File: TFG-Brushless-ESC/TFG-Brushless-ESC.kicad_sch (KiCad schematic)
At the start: 50 parts, among them J1 24V IN, J2 U, J3 V, J4 W, J5 USB C Receptacle, J6 HALL SENSORS, J7 SWD, SW1 BOOT0, SW2 NRST, U1 LM317, U2 LM317, U3 STM32F411CEUx, Y1 25MHz, Y2 32.768kHz

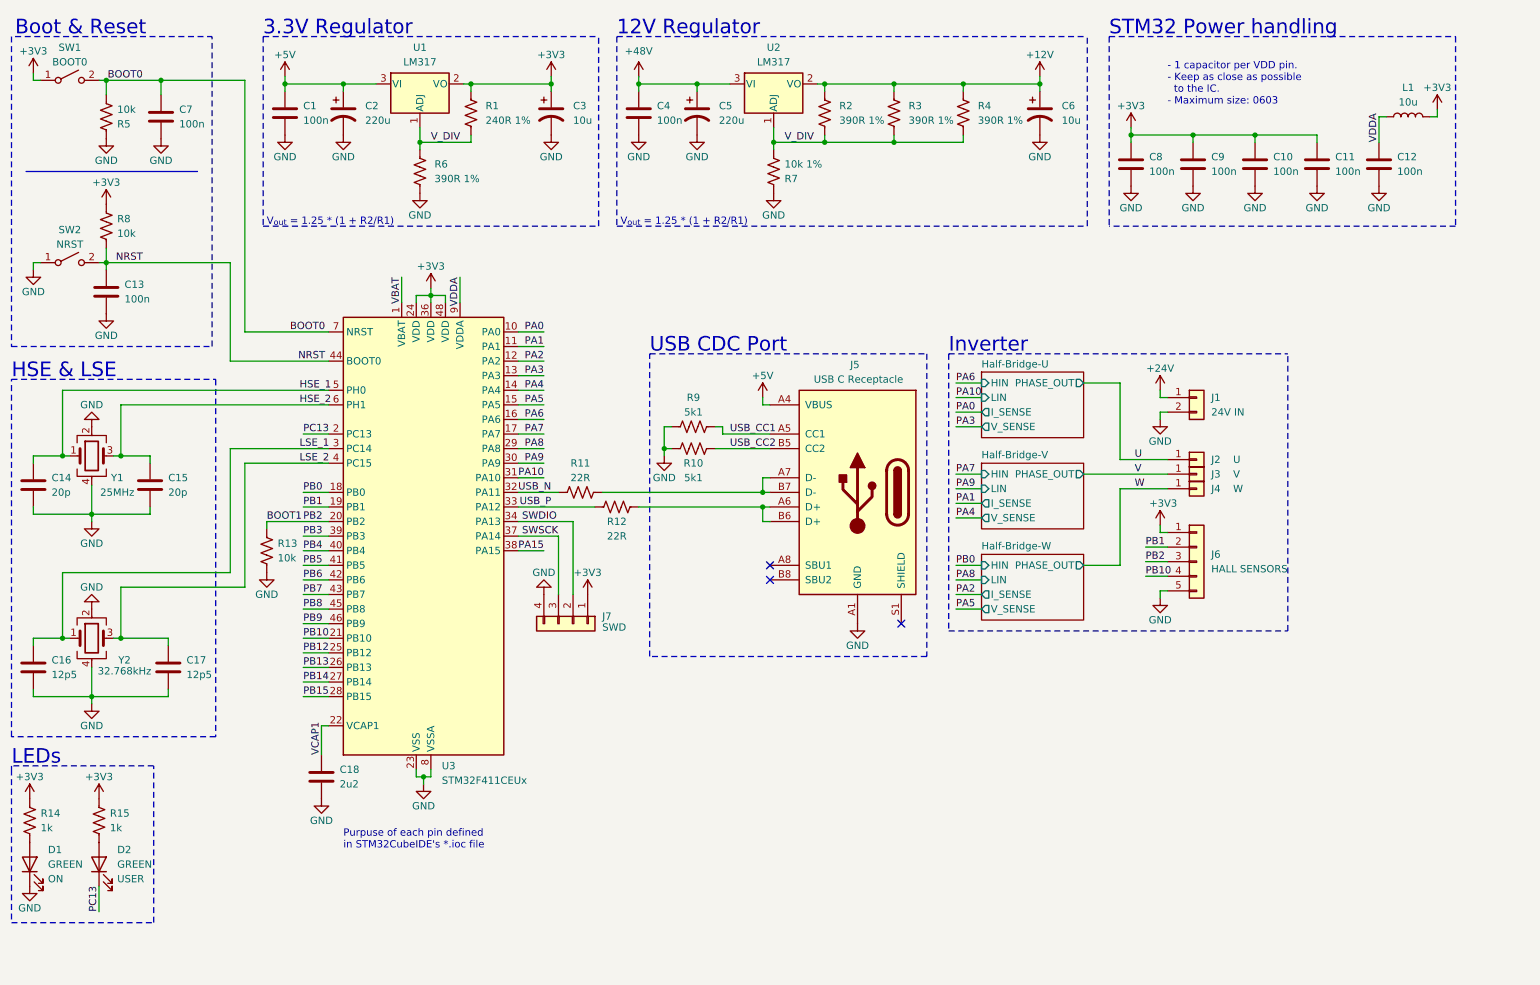
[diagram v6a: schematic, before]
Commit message: Switched stackup and routed part of uC
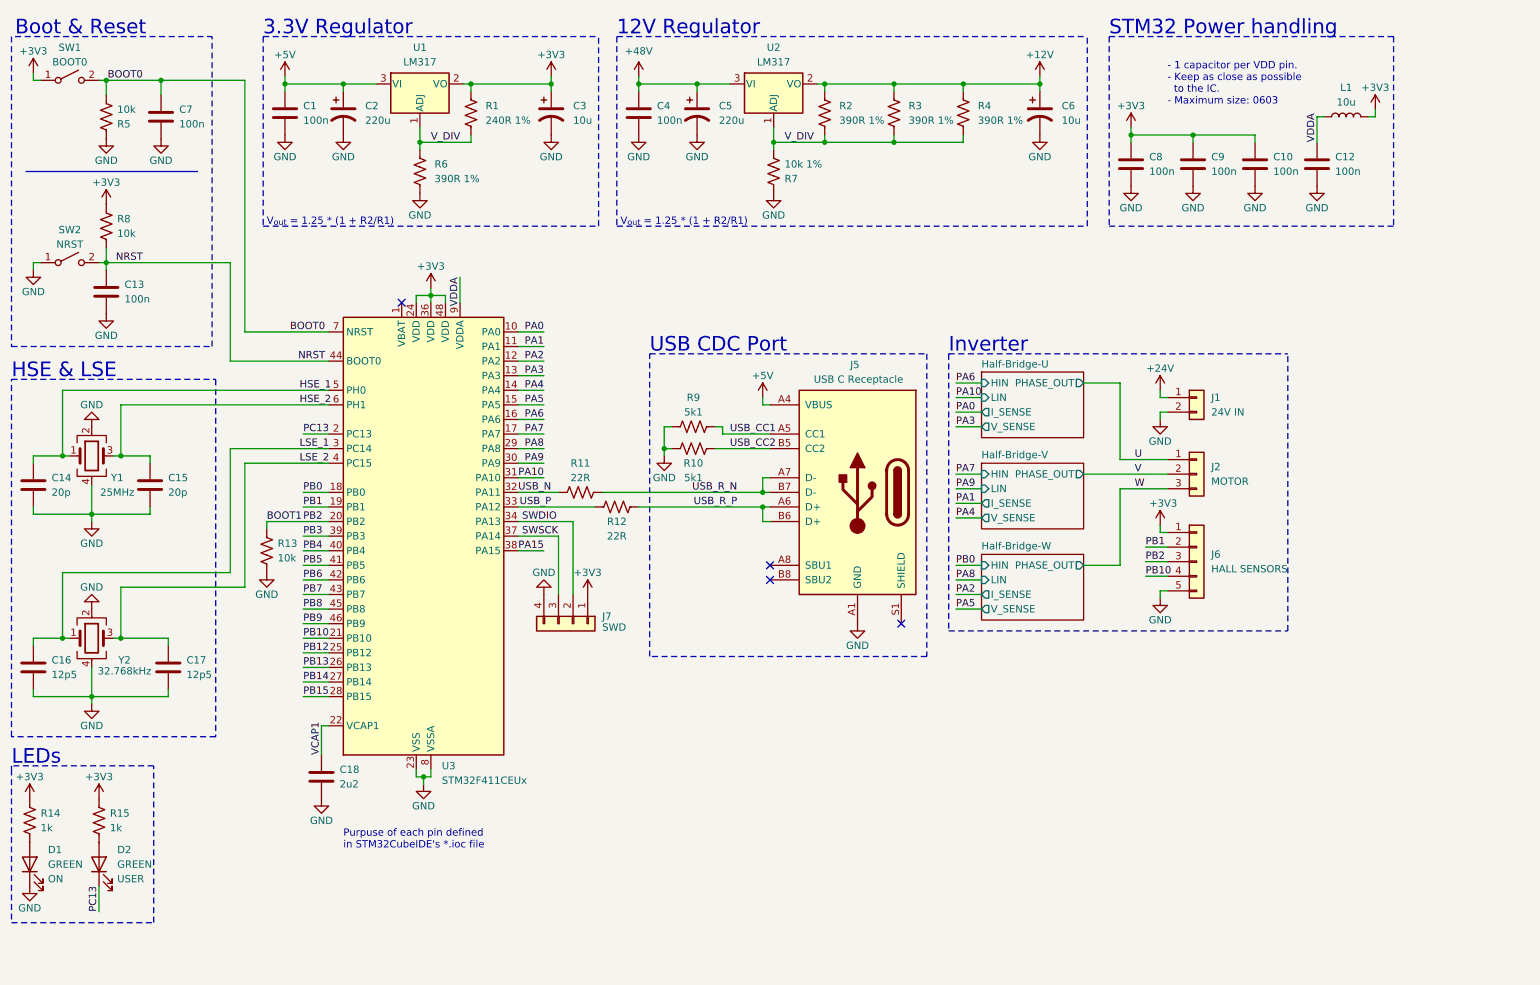
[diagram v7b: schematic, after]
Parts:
- removed C11: 100n, Capacitor_SMD:C_0603_1608Metric, symbol Device:C
- removed J2: U, TFG-Brushless-ESC:Large_Conn_01x01, symbol Connector_Generic:Conn_01x01
- removed J3: V, TFG-Brushless-ESC:Large_Conn_01x01, symbol Connector_Generic:Conn_01x01
- removed J4: W, TFG-Brushless-ESC:Large_Conn_01x01, symbol Connector_Generic:Conn_01x01
- added J2: MOTOR, TerminalBlock_Phoenix:TerminalBlock_Phoenix_MKDS-1,5-3-5.08_1x03_P5.08mm_Horizontal, symbol Connector_Generic:Conn_01x03
- J1: footprint TFG-Brushless-ESC:Large_Conn_01x02 -> TerminalBlock_Phoenix:TerminalBlock_Phoenix_MKDS-1,5-2-5.08_1x02_P5.08mm_Horizontal
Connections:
- net U: now also J2.1 (Pin_1)
- net V: now also J2.2 (Pin_2)
- net W: now also J2.3 (Pin_3)
- net USB_R_P: now reaches J5.A6 (D+), J5.B6 (D+), R12.2
- net USB_R_N: now reaches J5.A7 (D-), J5.B7 (D-), R11.2
- net VBAT: no longer names the net of U3.1 (VBAT)
- no-connect marks 3 -> 4
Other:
- moved on the sheet: C12, L1

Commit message: Changes in schematic and pcb
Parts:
- removed R13: 10k, Resistor_SMD:R_0603_1608Metric, symbol Device:R_US
- added C11, C43: 2u2, Capacitor_THT:CP_Radial_D5.0mm_P2.00mm, symbol Device:C_Polarized_US
- added D12: B240A-13-F, Diode_SMD:D_SMA, symbol Diode:1N4148W
- added D13: FERD30H100SB, Package_TO_SOT_SMD:TO-252-2, symbol Device:D_Schottky_AKA
- added D14, D15: SMAJ16CA-13-F, Diode_SMD:D_SMA, symbol Device:D_TVS
- added F1: 15 A, symbol Device:Fuse
- added F2: 2A, symbol Device:Polyfuse
- added R34, R35, R36: 10k, Resistor_SMD:R_0603_1608Metric, symbol Device:R_US
- J6: footprint Connector_PinHeader_2.54mm:PinHeader_1x05_P2.54mm_Vertical -> Connector_JST:JST_PH_B5B-PH-SM4-TB_1x05-1MP_P2.00mm_Vertical
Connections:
- net +48V is gone; now on net +24V: C4.1, C5.1, U2.3 (VI)
- net +12V: now also R4.2, R7.2, U2.1 (ADJ); no longer R2.1, R3.1, R4.1, U2.2 (VO)
- net +24V: now also C43.1, D13.2 (K); no longer J1.1 (Pin_1)
- net +3V3: now also R34.2, R35.2, R36.2
- net +5V: now also C11.1, D12.1 (K); no longer J5.A4 (VBUS), J5.A9 (VBUS), J5.B4 (VBUS), J5.B9 (VBUS)
- net GND: now also C11.2, C43.2, D14.1 (A1), D15.1 (A1)
- net PB1: now also R34.1
- net PB10: now also R36.1
- net BOOT1 renamed PB2
- net PB2: now also R35.1
- removed net V_DIV: R1.2, R2.2, R3.2, R4.2, R6.1, R7.2, U1.1 (ADJ), U2.1 (ADJ)
- new net: F1.1, J1.1 (Pin_1)
- new net: D13.1 (A), D13.3 (A), D14.2 (A2), F1.2
- new net: R2.1, U2.2 (VO)
- new net: R2.2, R3.1
- new net: R3.2, R4.1
- new net: D12.2 (A), D15.2 (A2), F2.2
- new net VDC: F2.1, J5.A4 (VBUS), J5.A9 (VBUS), J5.B4 (VBUS), J5.B9 (VBUS)
- new net V_DIV_3: R1.2, R6.1, U1.1 (ADJ)
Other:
- moved on the sheet: C10, C12, C6, C8, C9, J1, J6, L1, R2, R3, R4
